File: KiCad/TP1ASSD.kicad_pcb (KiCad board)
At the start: 2 copper layers, 200 x 50 mm, 67 parts, among them J1 Alimentacion, J10 JumperCtrlAS, J11 JumperCtrlSH, J2 GND, J3 Vi, J4 Jumper_FA, J5 Jumper_SH, J6 Jumper_AS, J7 Jumper_AS, J8 Vo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

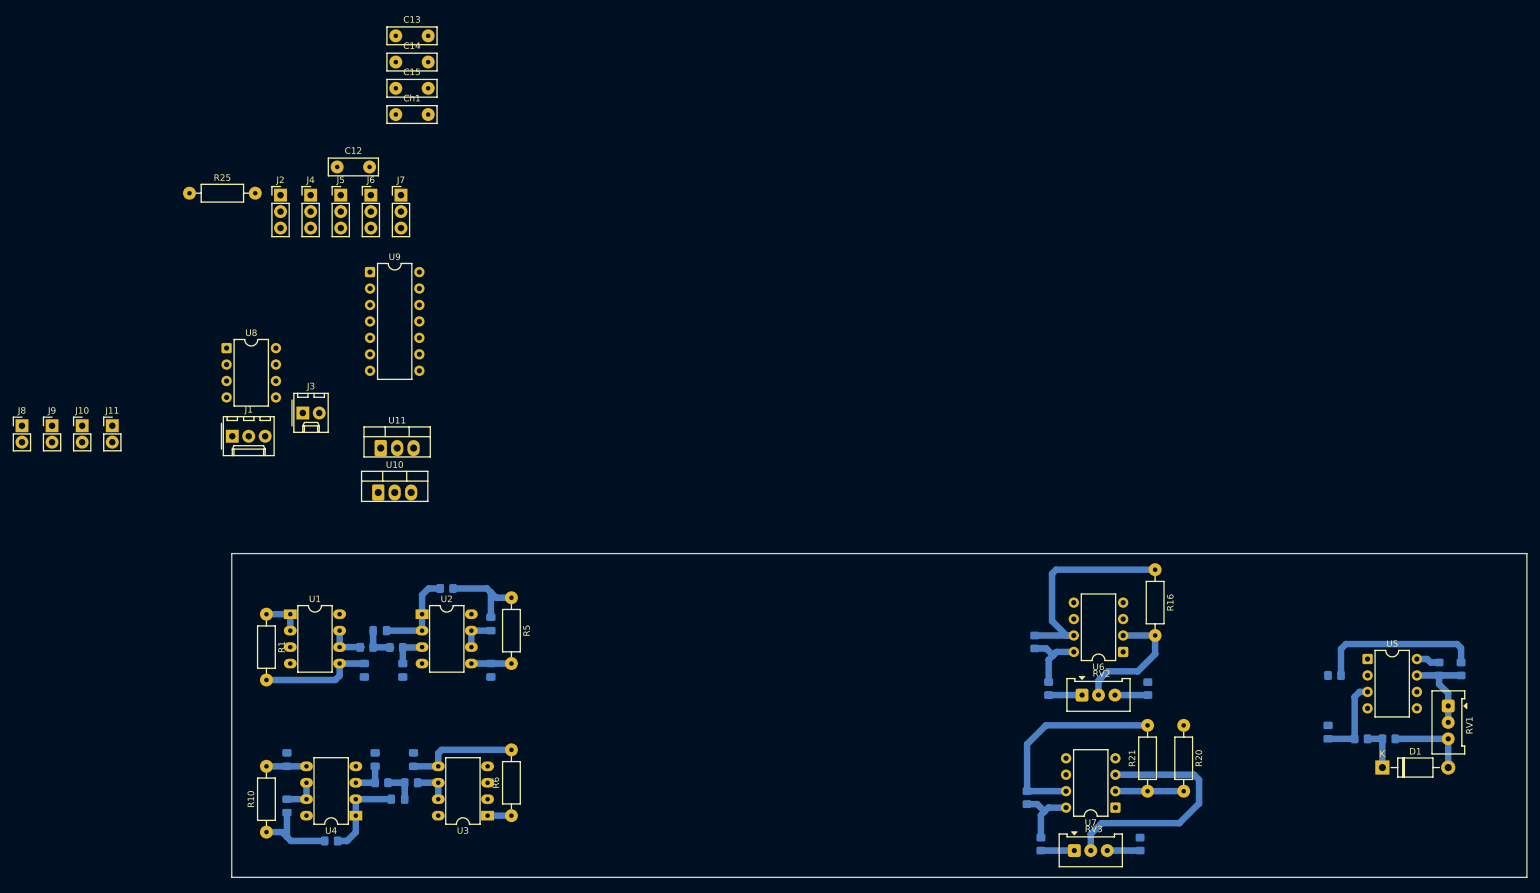
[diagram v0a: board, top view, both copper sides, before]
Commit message: ruteo del Sample and hold y de la llave
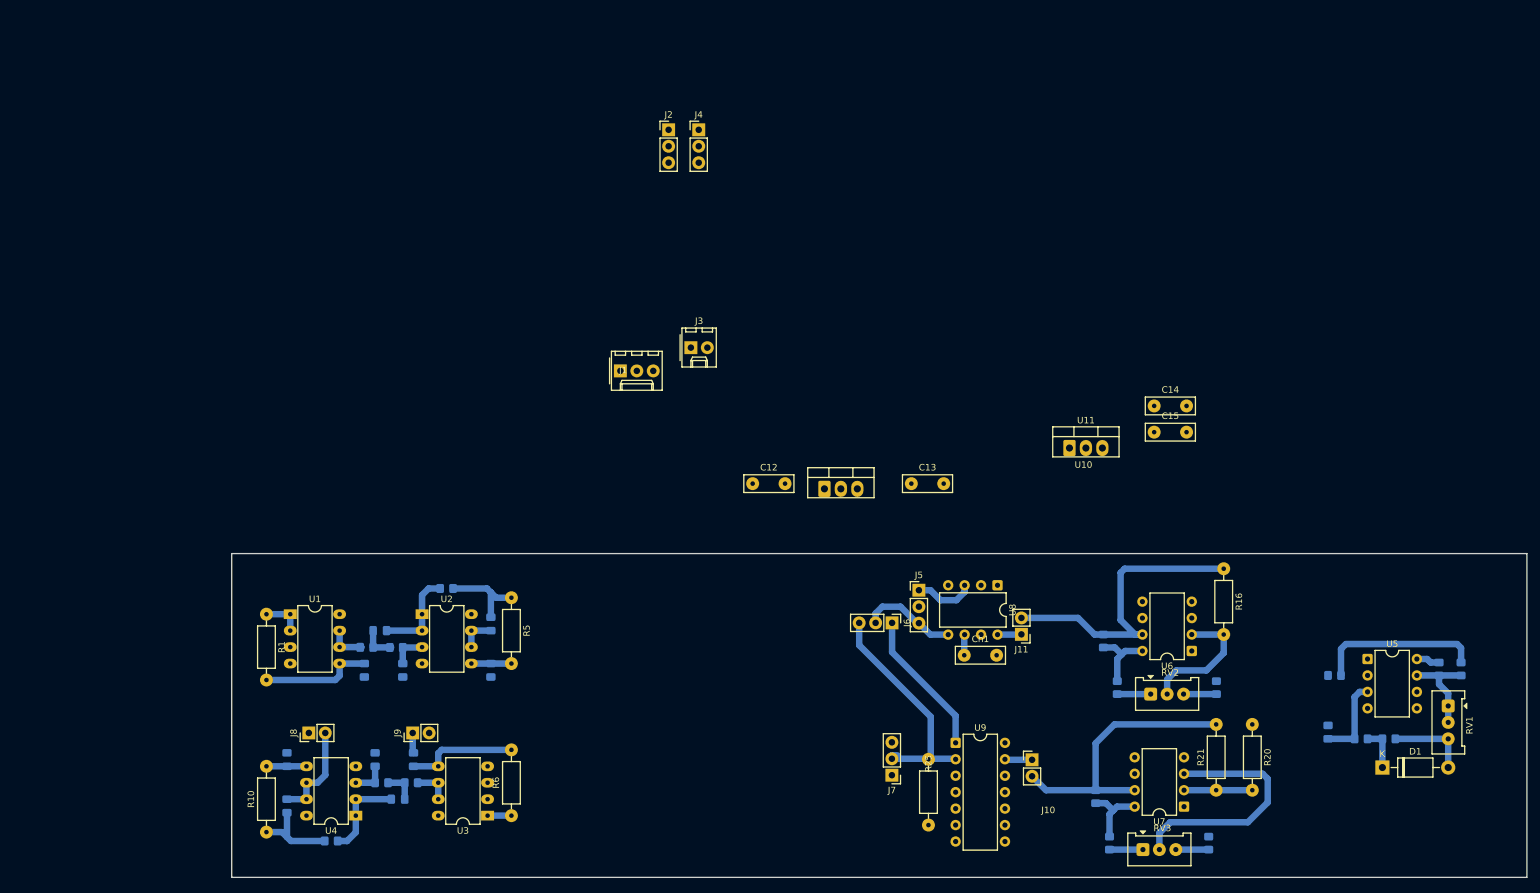
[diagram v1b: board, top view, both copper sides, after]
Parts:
- moved J10 155.5 mm to (176.6, 133.1)
- moved J11 144.0 mm to (175.0, 113.8), turned to 180 degrees
- moved R25 143.7 mm to (160.6, 133.1), turned to -90 degrees
- moved C14 128.6 mm to (195.5, 78.5)
- moved C15 128.6 mm to (195.5, 82.5)
- moved U8 124.6 mm to (171.3, 106.2), turned to -90 degrees
- moved Ch1 121.2 mm to (166.2, 117.0)
- moved J7 117.3 mm to (155.0, 135.5), turned to 180 degrees
- moved U9 116.0 mm to (164.8, 130.5)
- moved J5 108.1 mm to (159.2, 107.0)
- moved U11 106.4 mm to (182.4, 85.0)
- moved C13 105.4 mm to (158.0, 90.5)
- moved J6 104.1 mm to (155.0, 112.0), turned to -90 degrees
- moved C12 80.7 mm to (133.5, 90.5)
- moved J9 73.2 mm to (81.0, 129.0), turned to 90 degrees
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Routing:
- net /Vo_AS: track 0.00 -> 37.0 mm
- net /Vi_AS: track 0.00 -> 22.6 mm
- net /Vo_SH: track 0.00 -> 14.9 mm
- net /SH_ctrl: track 33.8 -> 47.5 mm
- net /AS_ctrl: track 33.1 -> 43.8 mm
- net /Vo_FR: track 5.55 -> 15.4 mm
- net /Vi_SH: track 0.00 -> 9.26 mm
- net Net-(J10-Pad1): track 0.00 -> 4.22 mm
- net Net-(U8-Hold): track 0.00 -> 3.71 mm
- net Net-(U8-C_{h}): track 0.00 -> 3.21 mm
- net GND: track 0.00 -> 3.16 mm

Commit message: Acomode la bottom y agregue el plano de masa abajo. Creo que ya esta ruteado todo lo signal-related.
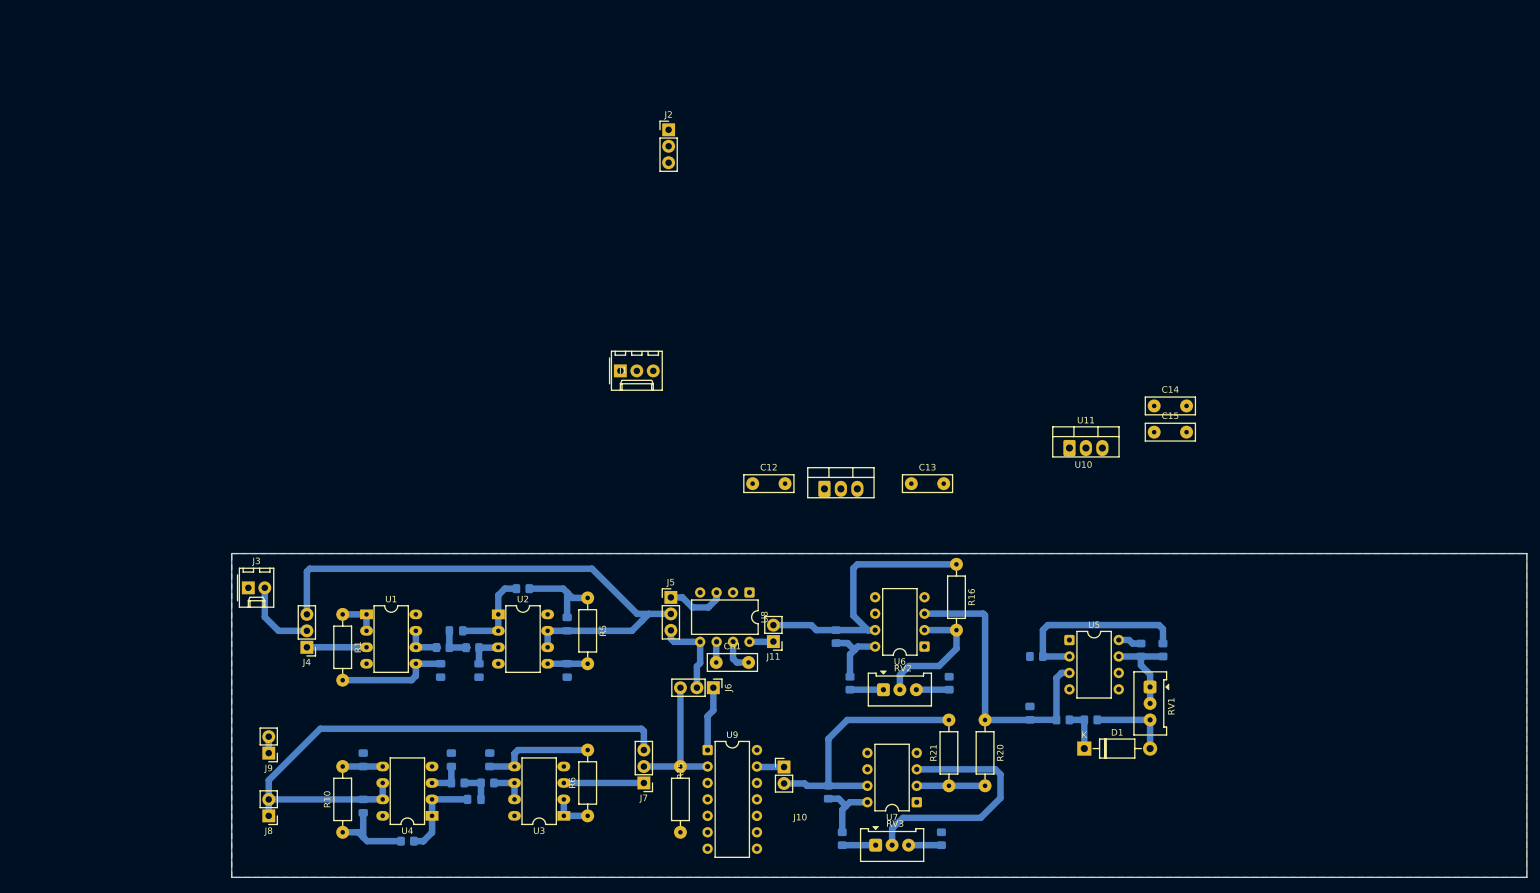
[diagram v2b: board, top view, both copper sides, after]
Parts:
- moved J4 100.2 mm to (64.7, 115.8), turned to 180 degrees
- moved J3 77.8 mm to (55.6, 106.6)
- moved C11 46.1 mm to (176.3, 125.9)
- moved D1 46.1 mm to (184.7, 131.4)
- moved R11 46.1 mm to (196.9, 116.2)
- moved R12 46.1 mm to (177.3, 117.2)
- moved R13 46.1 mm to (193.5, 116.2)
- moved R14 46.1 mm to (185.7, 127.0)
- moved R15 46.1 mm to (181.4, 127.0)
- moved RV1 46.1 mm to (194.9, 121.9)
- moved U5 46.1 mm to (182.4, 114.7)
- moved R16 41.3 mm to (165.0, 103.0)
- moved R17 41.3 mm to (146.4, 114.1)
- moved R18 41.3 mm to (148.5, 121.3)
- moved R19 41.3 mm to (163.8, 121.3)
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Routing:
- net /Vo_FA: track 5.55 -> 85.1 mm
- net /Vo_FR: track 15.4 -> 89.9 mm
- net Net-(U5--): track 12.9 -> 45.4 mm
- net /Vo_AS: track 37.0 -> 22.0 mm
- net /Vi_AS: track 22.6 -> 9.99 mm
- net /Vi_FR: track 0.00 -> 12.4 mm
- net /Vi: track 0.00 -> 11.9 mm
- net /Vi_FA: track 0.00 -> 9.21 mm
- net GND: track 3.16 -> 7.94 mm
- net Net-(U5-+): track 25.4 -> 29.5 mm
- net /SH_ctrl: track 47.5 -> 43.8 mm
- net /AS_ctrl: track 43.8 -> 40.1 mm
- net Net-(U3A--): track 3.68 -> 6.22 mm
- net /Vo_SH: track 14.9 -> 13.6 mm
- added copper zone on B.Cu, net GND

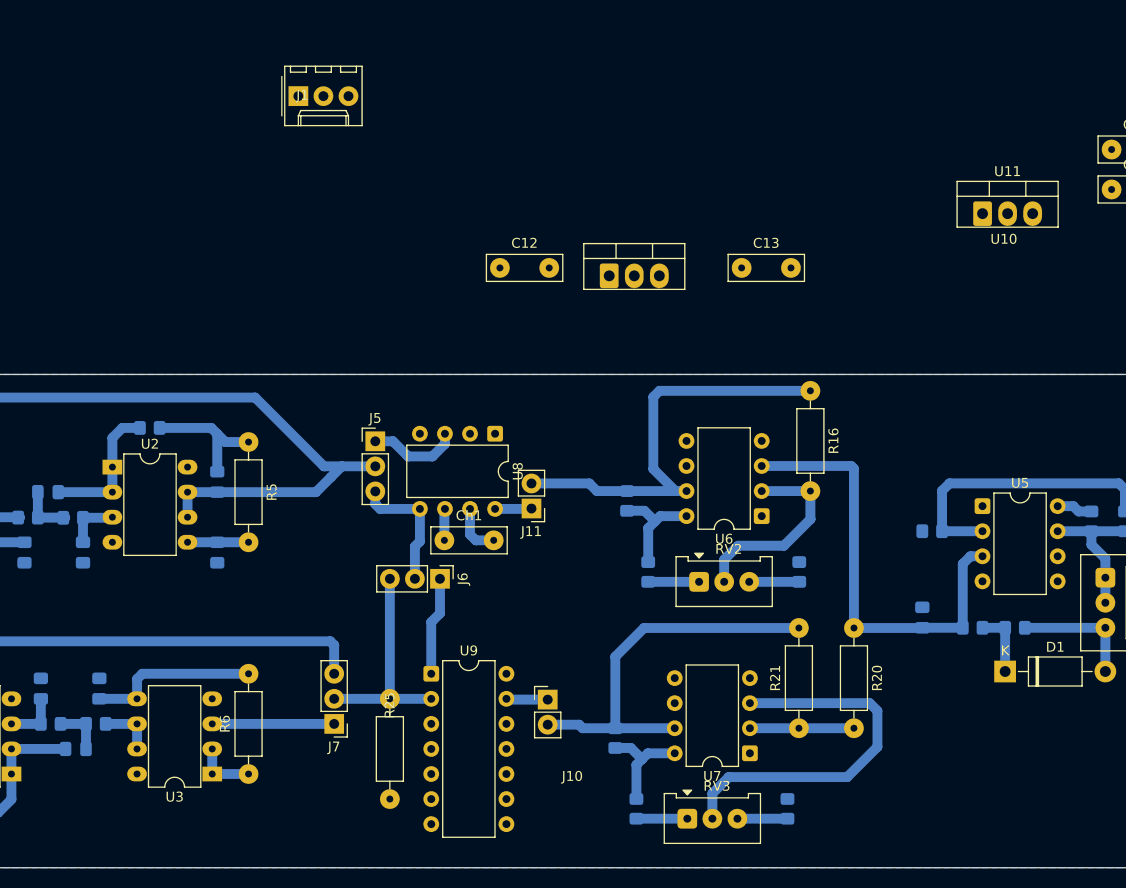
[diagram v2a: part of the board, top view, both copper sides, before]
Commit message: Agregue capas de desacople y DC zerooing para el SH
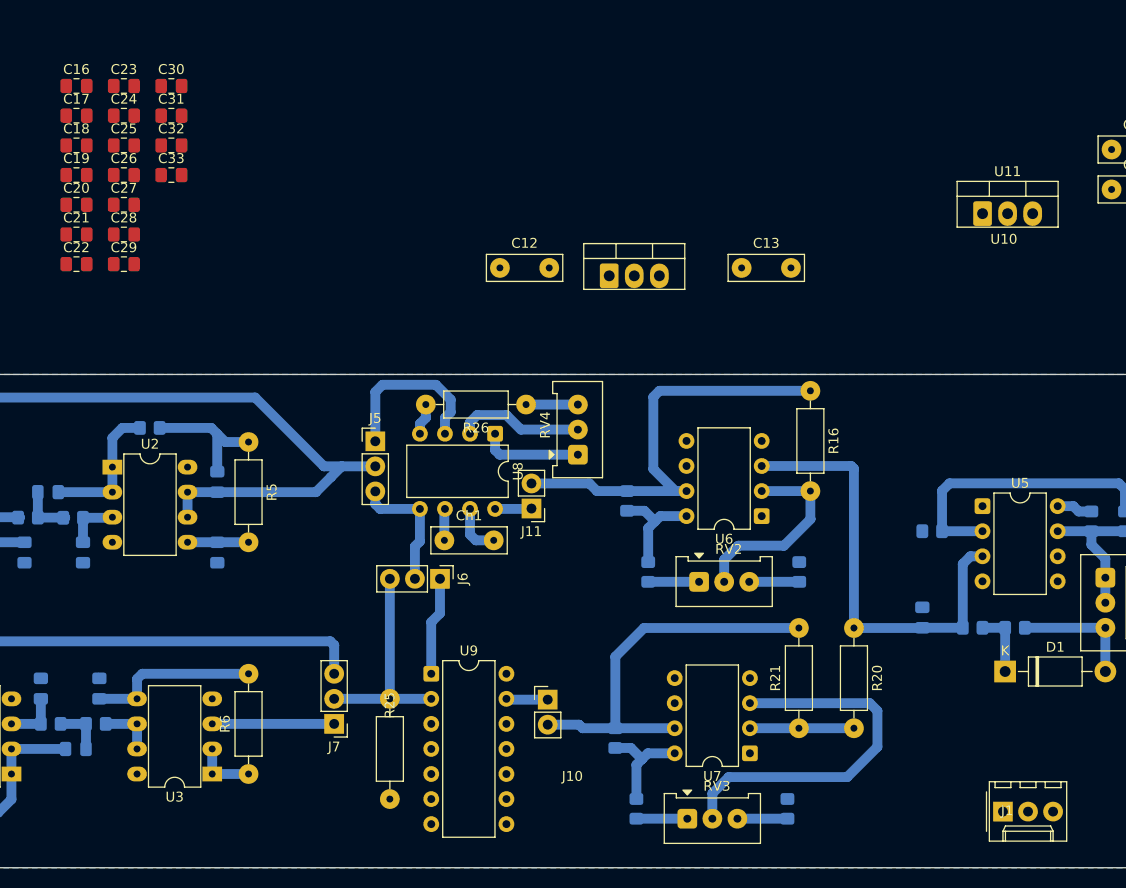
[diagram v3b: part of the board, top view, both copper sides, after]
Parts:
- added C16: 100n, TCLib:C_0805, F.Cu at (90.6, 72.1)
- added C17: 100n, TCLib:C_0805, F.Cu at (90.6, 75.1)
- added C18: 100n, TCLib:C_0805, F.Cu at (90.6, 78.1)
- added C19: 100n, TCLib:C_0805, F.Cu at (90.6, 81.1)
- added C20: 100n, TCLib:C_0805, F.Cu at (90.6, 84.1)
- added C21: 100n, TCLib:C_0805, F.Cu at (90.6, 87.1)
- added C22: 100n, TCLib:C_0805, F.Cu at (90.6, 90.1)
- added C23: 100n, TCLib:C_0805, F.Cu at (95.4, 72.1)
- added C24: 100n, TCLib:C_0805, F.Cu at (95.4, 75.1)
- added C25: 100n, TCLib:C_0805, F.Cu at (95.4, 78.1)
- added C26: 100n, TCLib:C_0805, F.Cu at (95.4, 81.1)
- added C27: 100n, TCLib:C_0805, F.Cu at (95.4, 84.1)
- added C28: 100n, TCLib:C_0805, F.Cu at (95.4, 87.1)
- added C29: 100n, TCLib:C_0805, F.Cu at (95.4, 90.1)
- added C30: 100n, TCLib:C_0805, F.Cu at (100.2, 72.1)
- added C31: 100n, TCLib:C_0805, F.Cu at (100.2, 75.1)
- added C32: 100n, TCLib:C_0805, F.Cu at (100.2, 78.1)
- added C33: 100n, TCLib:C_0805, F.Cu at (100.2, 81.1)
- added R26: 33k, TCLib:R_0.25W, F.Cu at (136.2, 104.3)
- added RV4: 1k, TCLib:RV_Preset_multivuelta_10mm_5mm, F.Cu at (141.4, 109.4)
- moved J1 101.8 mm to (184.5, 145.6)
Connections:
- U8 pad 2: unconnected-(U8-Adj-Pad2) -> Net-(U8-Adj)
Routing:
- net Net-(U8-Adj): track 0.00 -> 13.0 mm
- net +10V: track 3.64 -> 13.9 mm
- net /Vi_SH: track 9.26 -> 17.3 mm
- net Net-(R26-Pad1): track 0.00 -> 5.25 mm
- net -10V: track 0.00 -> 3.22 mm
